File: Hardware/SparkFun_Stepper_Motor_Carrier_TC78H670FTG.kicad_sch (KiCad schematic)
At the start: 16 parts, among them J1 Conn_01x08, J2 Conn_01x08

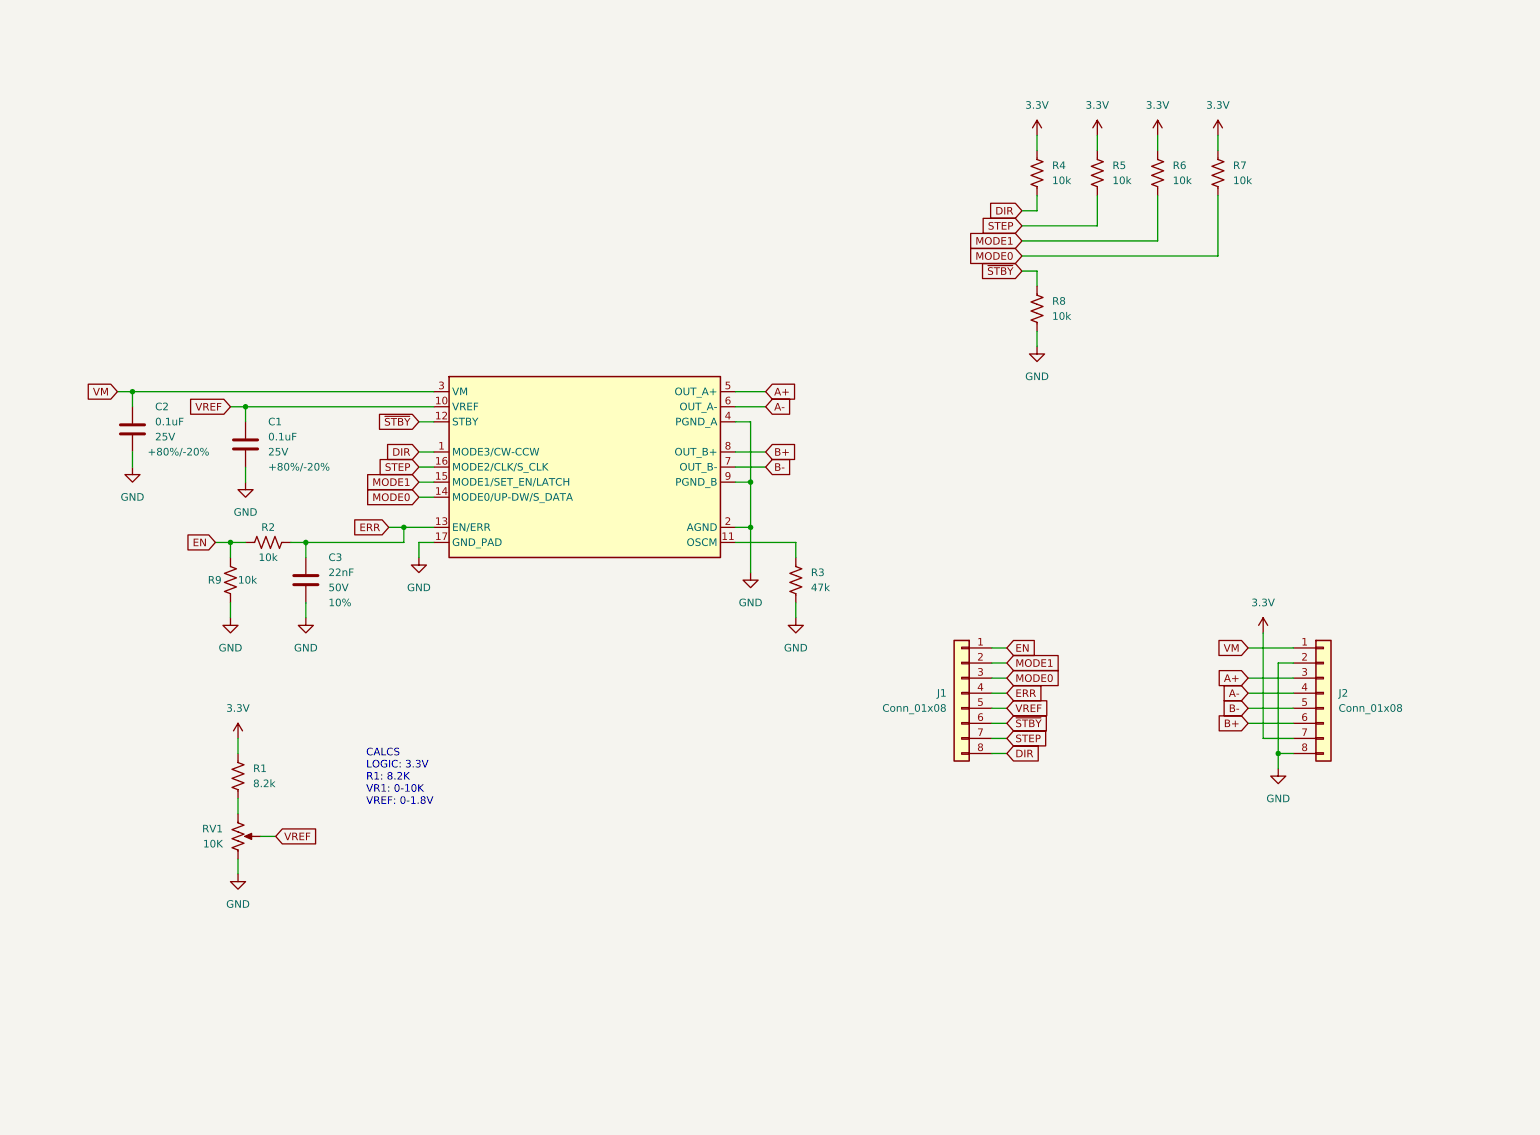
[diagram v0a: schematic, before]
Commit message: review notes round 1
-SCH
--general cleanup
--fiducials
--section lines
--SFE logo
--OSHW logo
--voltage and current rating
--showing U1 reference and value
-BOARD
--flipped version number on board
--designer name
--ordering instructions
--CC license
--SFE logo
--oshw logo
--polygon clearnaces set to 0.2032mm
--removed unncessary gnd vias
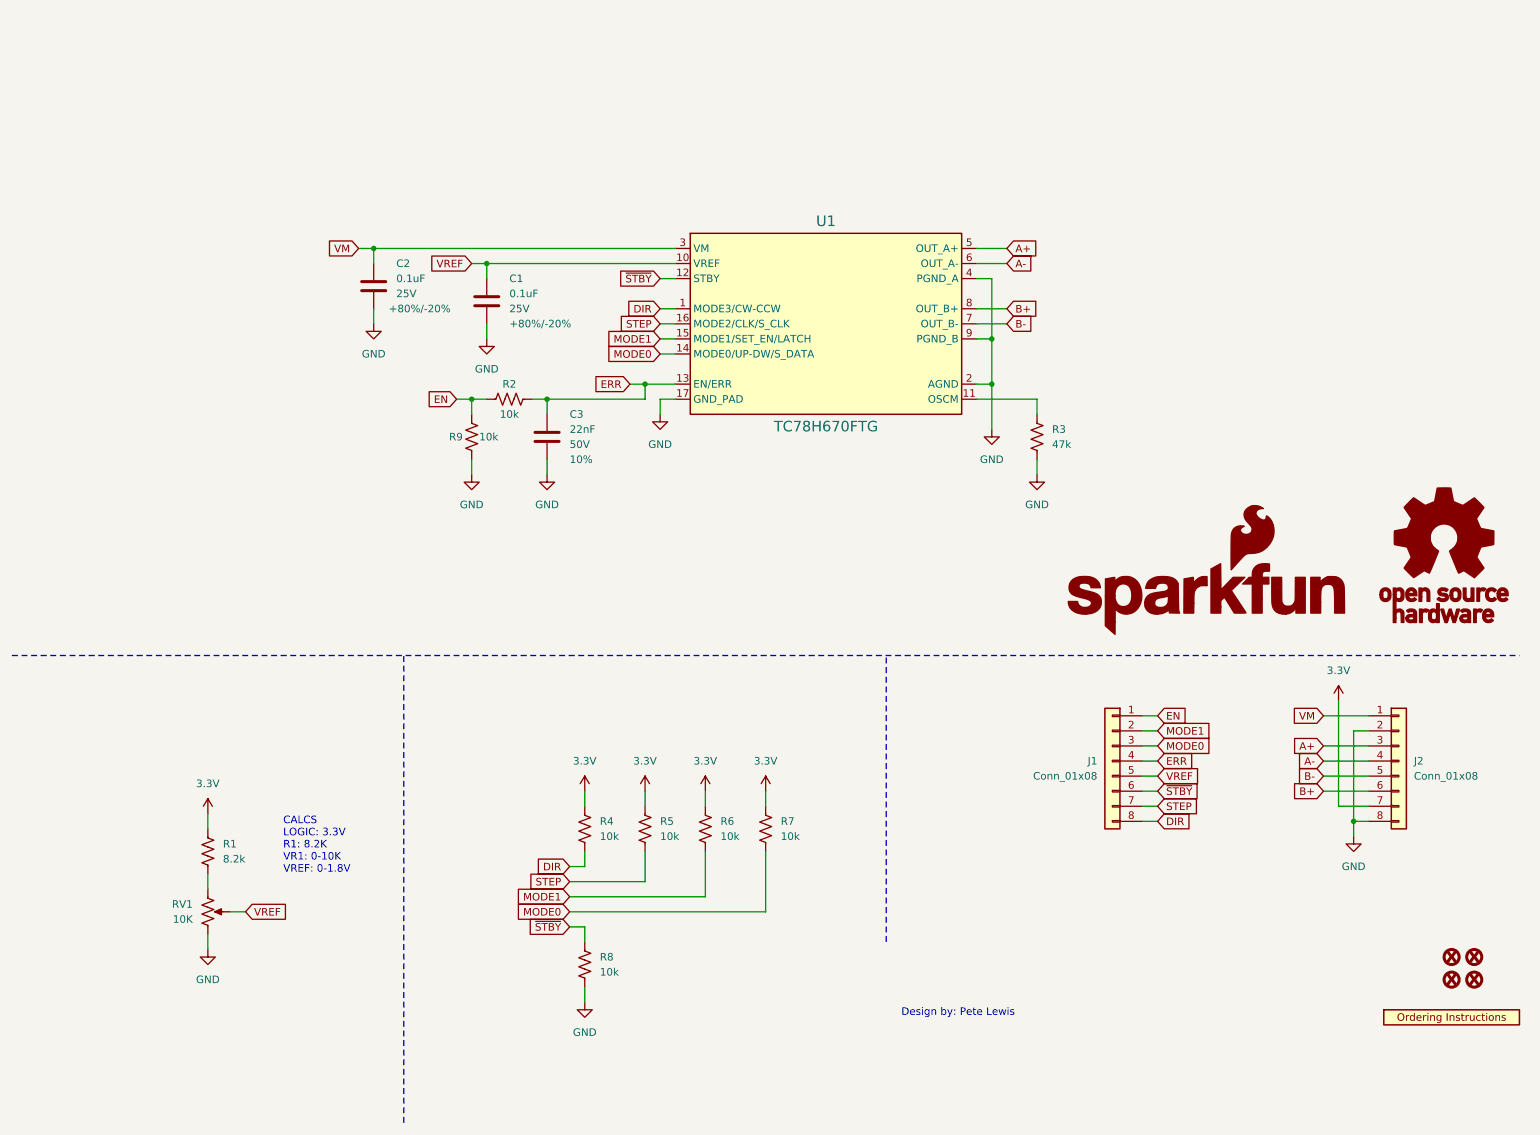
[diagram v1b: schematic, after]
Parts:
- added FID1, FID2, FID3, FID4: Fiducial_0.5mm, SparkFun-Aesthetic:Fiducial_0.5mm_Mask1mm, symbol SparkFun-Aesthetic:Fiducial_0.5mm
- added G1: OSHW_Logo, SparkFun-Aesthetic:Creative_Commons_License, symbol SparkFun-Aesthetic:OSHW_Logo
- added G2: SparkFun_Logo, symbol SparkFun-Aesthetic:SparkFun_Logo
- added U2: ~, SparkFun-Aesthetic:ORDERING_INSTRUCTIONS, symbol SparkFun-Aesthetic:Ordering_Instructions
- U1: value ~ -> TC78H670FTG
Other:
- note added: "Design by: Pete Lewis"
- moved on the sheet: C1, C2, C3, J1, J2, R1, R2, R3, R4, R5, R6, R7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

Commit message: sch max voltage note
-and more gitignore
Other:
- note added: "Power supply (VM) operating voltage: 2.5V to 16.0V Output Current ratings: 2.0 A (max) Logic Level 5.5V tolerant Logic LOW Threshold: 0.7V Logic HIGH Threshold: 1.5V"
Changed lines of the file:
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@@
+    (effects (font (size 1.27 1.27)) (justify left bottom))
+  )
+  (text "Power supply (VM) operating voltage: 2.5V to 16.0V\nOutput Current ratings: 2.0 A (max)\nLogic Level 5.5V tolerant\nLogic LOW Threshold: 0.7V\nLogic HIGH Threshold: 1.5V"
+    (at 127 40.64 0)
     (effects (font (size 1.27 1.27)) (justify left bottom))
   )

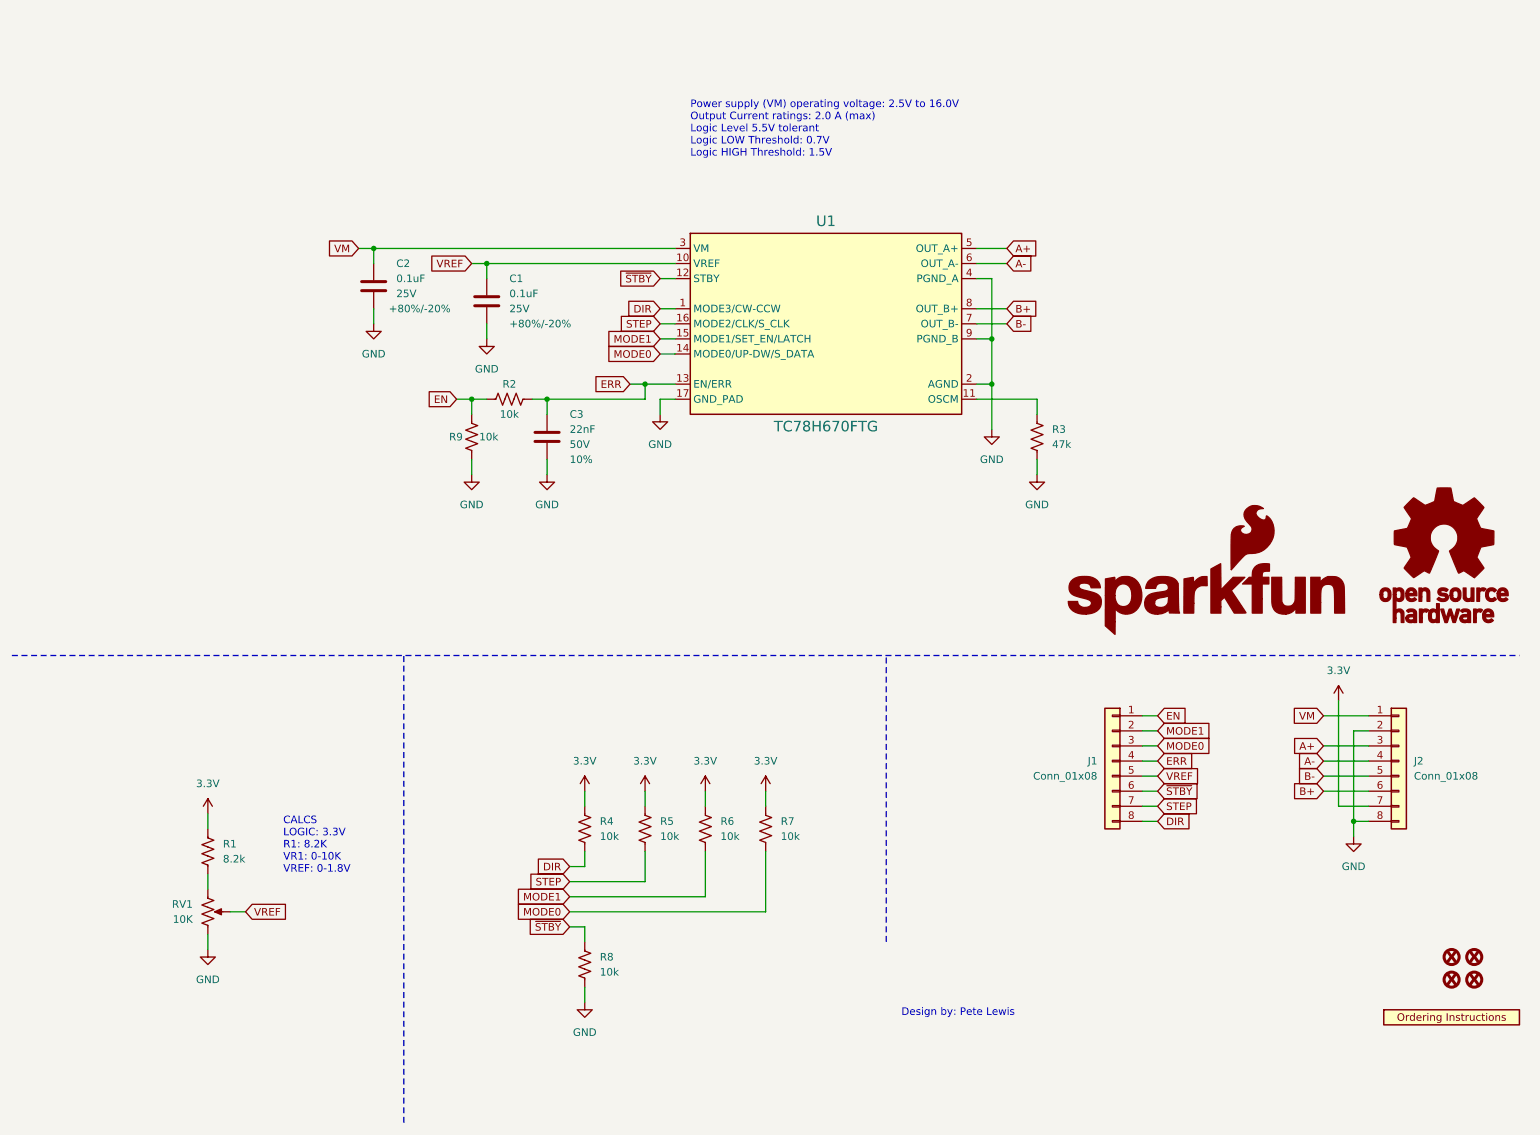
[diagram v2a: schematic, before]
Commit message: schematic cleanup
-section titles
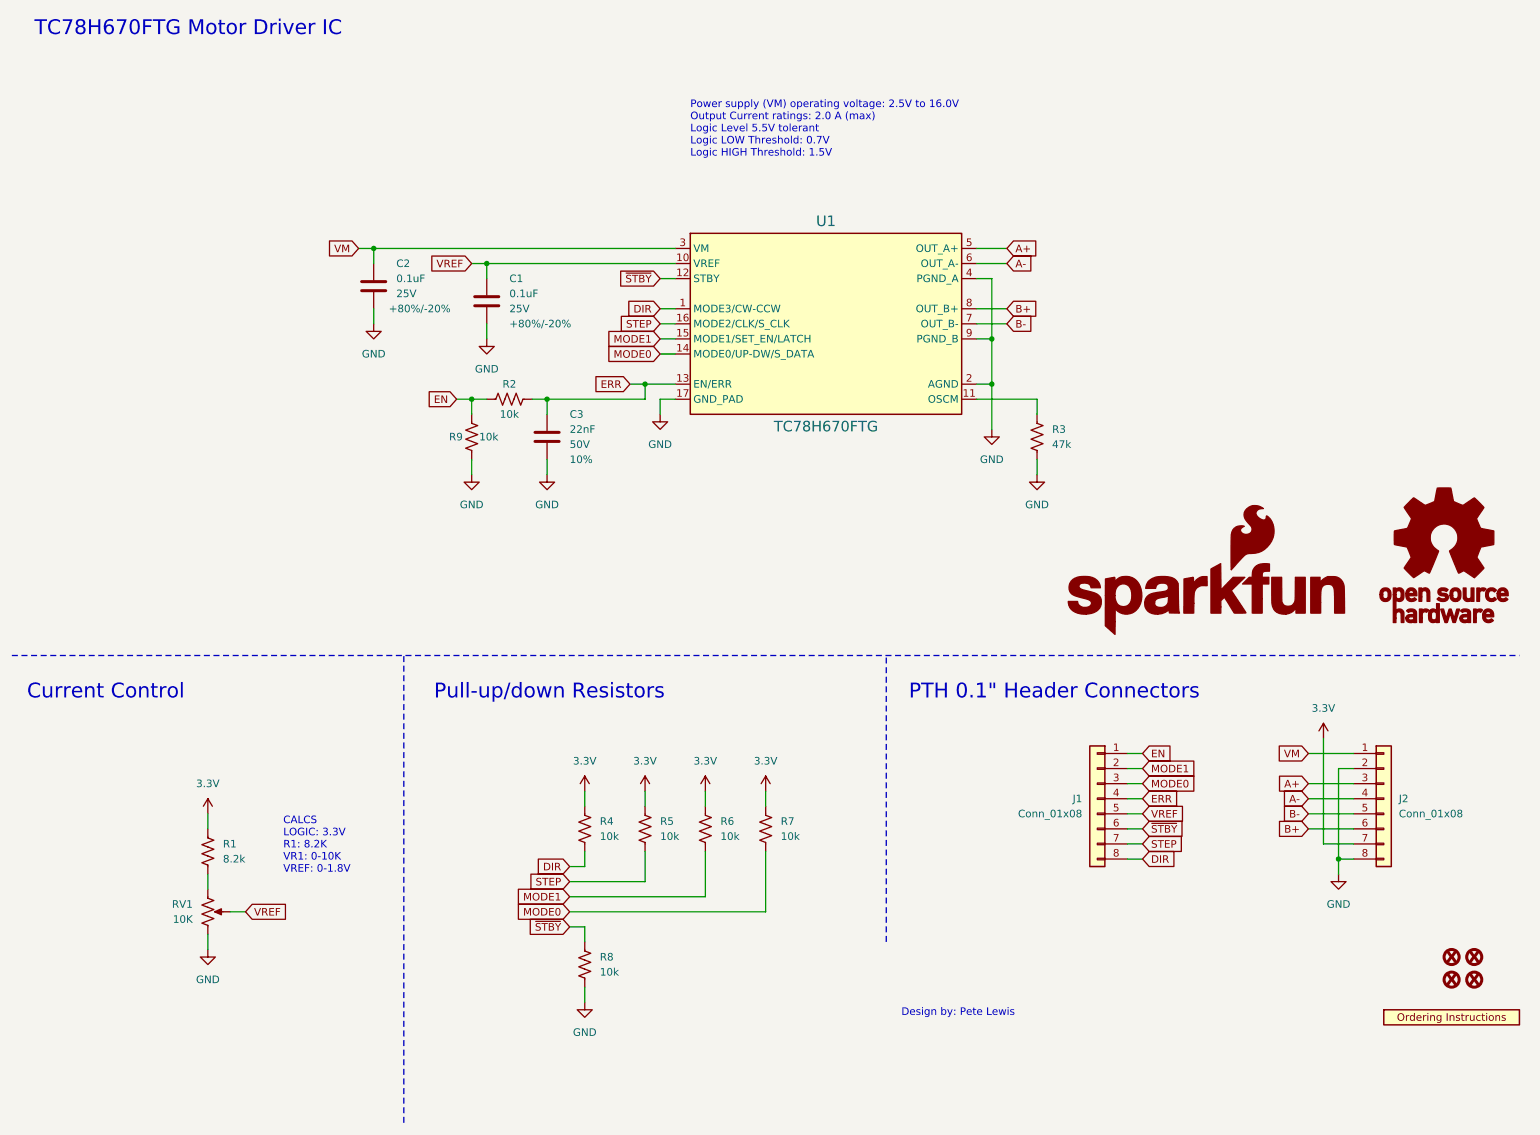
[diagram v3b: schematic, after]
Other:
- note added: "Current Control"
- note added: "PTH 0.1" Header Connectors"
- note added: "Pull-up/down Resistors"
- note added: "TC78H670FTG Motor Driver IC"
- moved on the sheet: J1, J2

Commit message: more stuff pre-review
-copper weight added to ordering instructions
-removed old sym library from project table (eagle import from older prodriver)
-added CC license to sch
-added M2 and M3 to buzzard labels for STEP and DIR
-copper edge clearance in DRC set to 0.2mm
-excluded DRC errors that I wish to ignore
-used one signle GND zone for top in1 and bottom copper ground pours
-adjusted clearances/min-widths/spoke-thickness/DRC to get ideal GND zone flow.
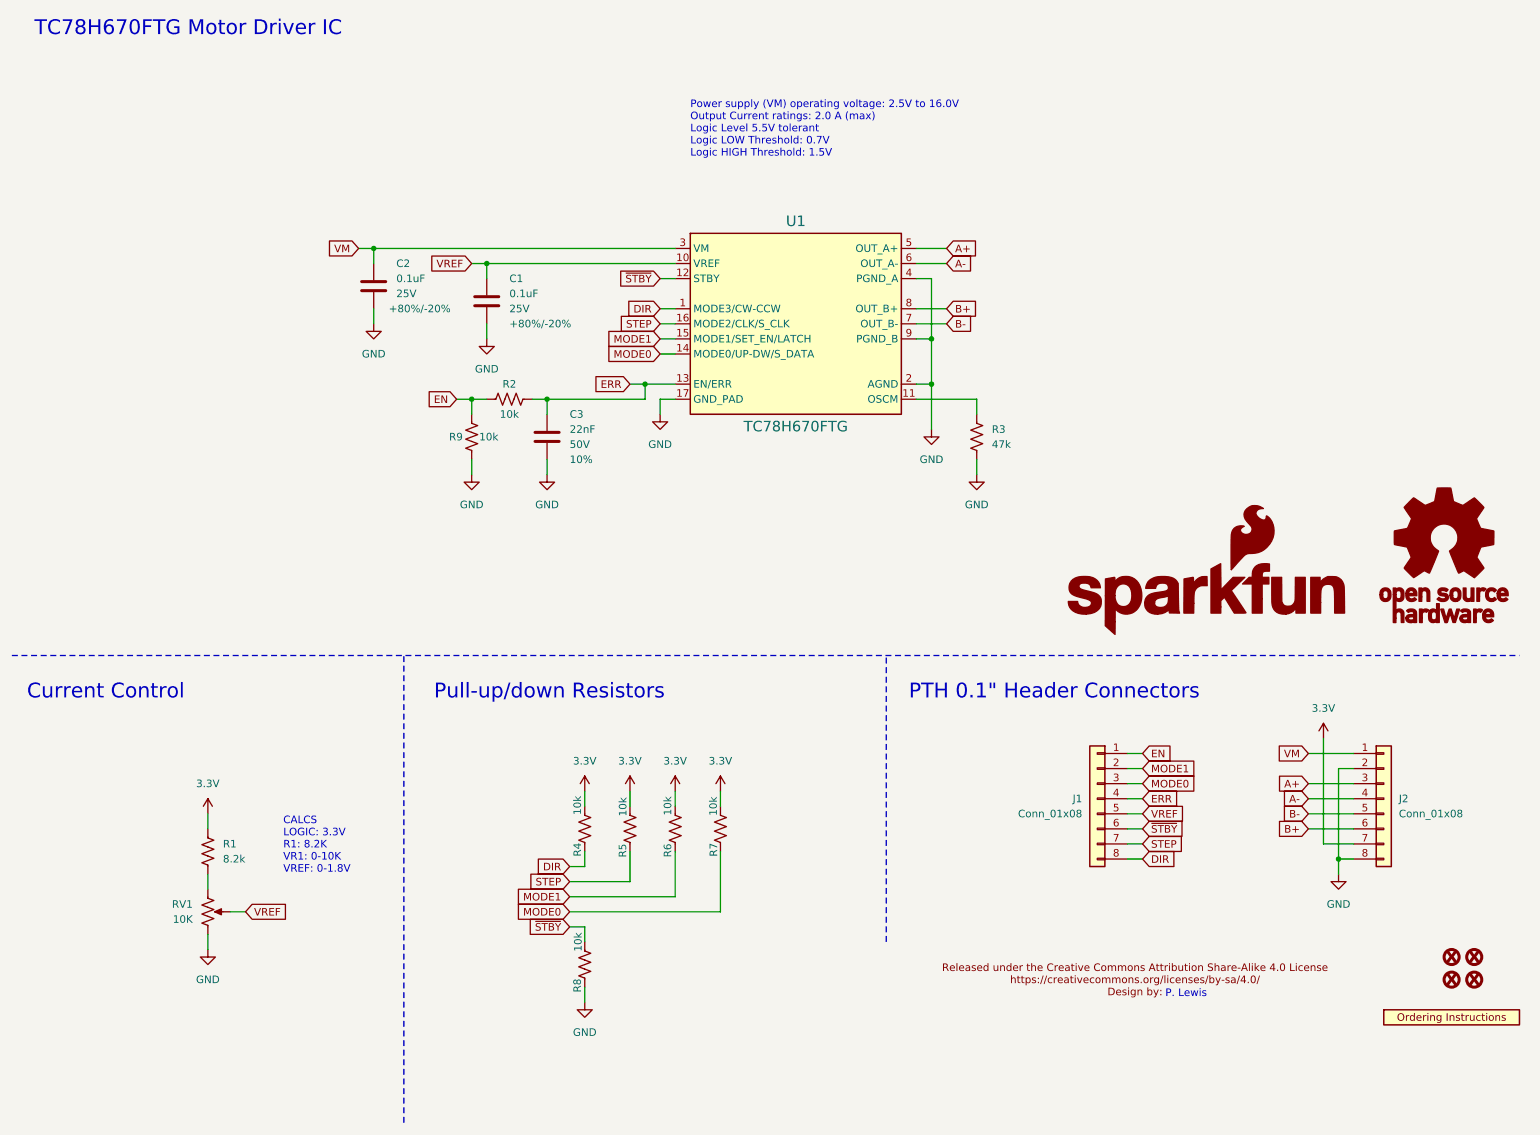
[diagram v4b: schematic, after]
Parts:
- added ref**1: val**, SparkFun-Aesthetic:Creative_Commons_License, symbol SparkFun-Aesthetic:Creative_Commons_License
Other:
- note added: "P. Lewis"
- note removed: "Design by: Pete Lewis"
- moved on the sheet: R3, R5, R6, R7, U1
